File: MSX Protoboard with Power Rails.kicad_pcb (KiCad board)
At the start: 2 copper layers, 103 x 66 mm, 806 parts

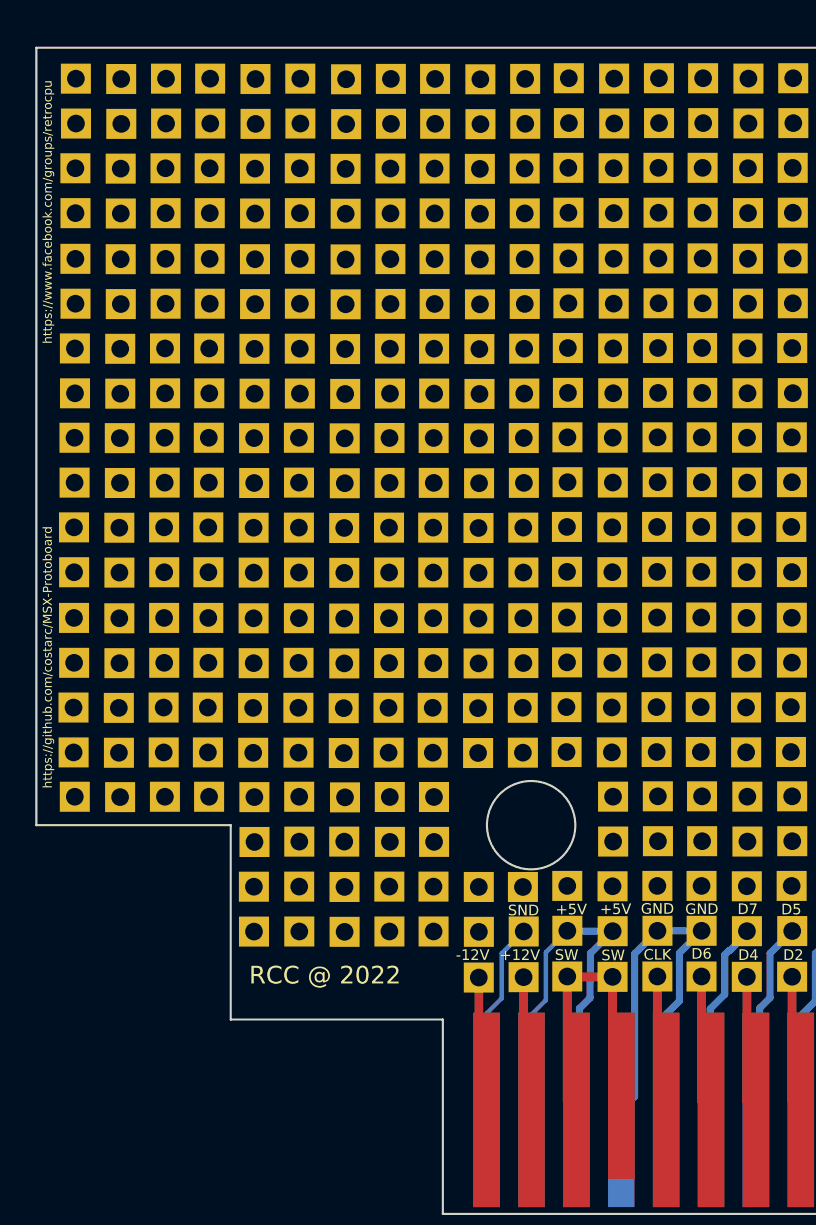
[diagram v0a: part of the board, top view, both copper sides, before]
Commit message: Added a version with power rails +5v / gnd for convenience
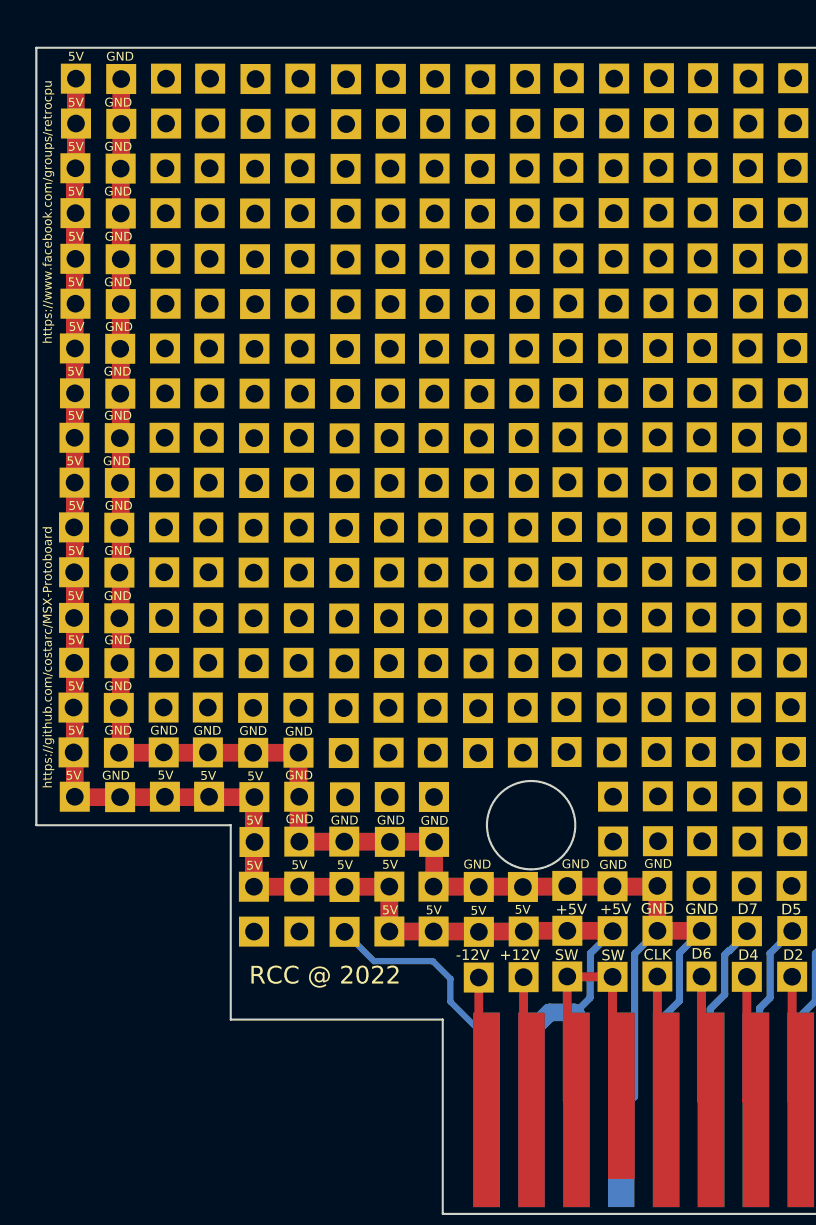
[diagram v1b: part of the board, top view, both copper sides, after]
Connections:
- ? pad 76: (no net) -> +5V (x29)
- ? pad 76: (no net) -> GNDREF (x31)
- ? pad 76: SOUNDIN -> +5V
- ? pad 76: (no net) -> SOUNDIN
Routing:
- net GNDREF: track 24.5 -> 103.3 mm
- net +5V: track 24.5 -> 102.7 mm
- net SOUNDIN: track 11.0 -> 15.4 mm
- net SW1: track 18.1 -> 17.4 mm
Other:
- board text added: "5V"
- board text removed: "SND"
